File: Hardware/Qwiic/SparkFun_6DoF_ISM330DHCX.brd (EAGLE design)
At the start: 25.4 x 25.4 mm, 64 parts, among them J1 QWIIC_RIGHT_ANGLE, J2 QWIIC_RIGHT_ANGLE, U1 ISM330DHCX

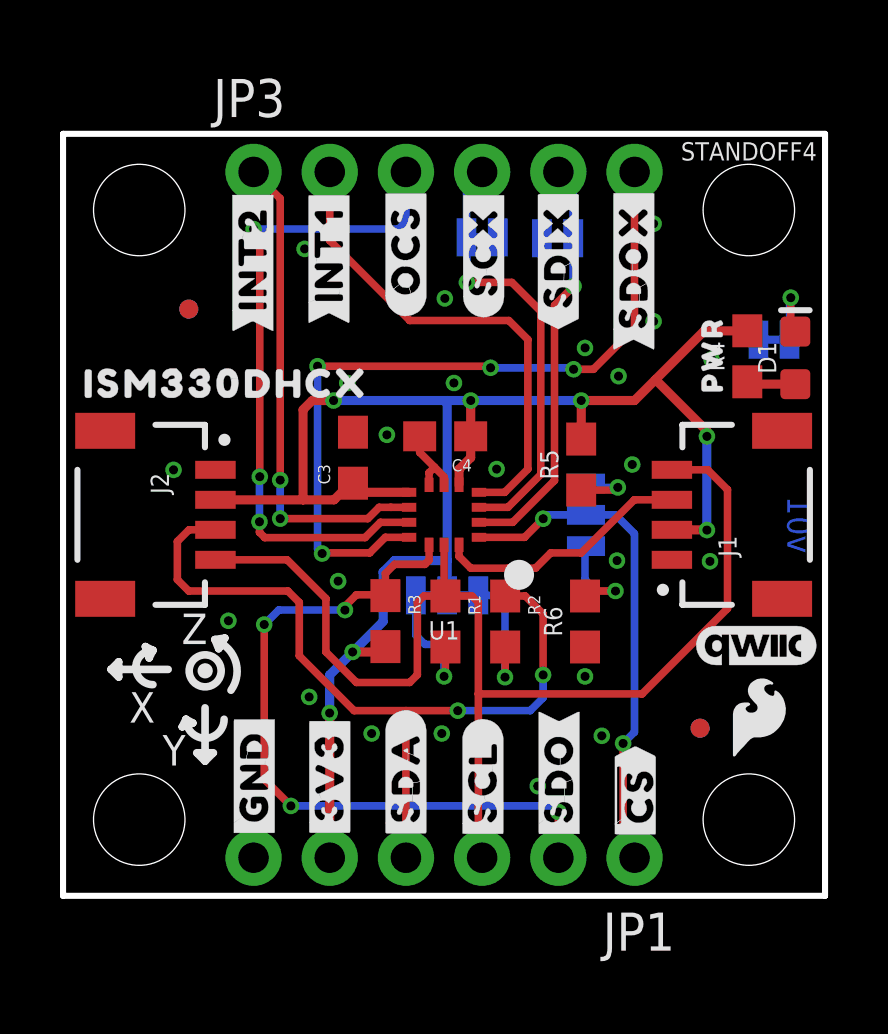
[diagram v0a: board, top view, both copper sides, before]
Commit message: Updates labels on 1x1 to new SPI nomenclature,
* moves pin1 indicator on IC closer to IC
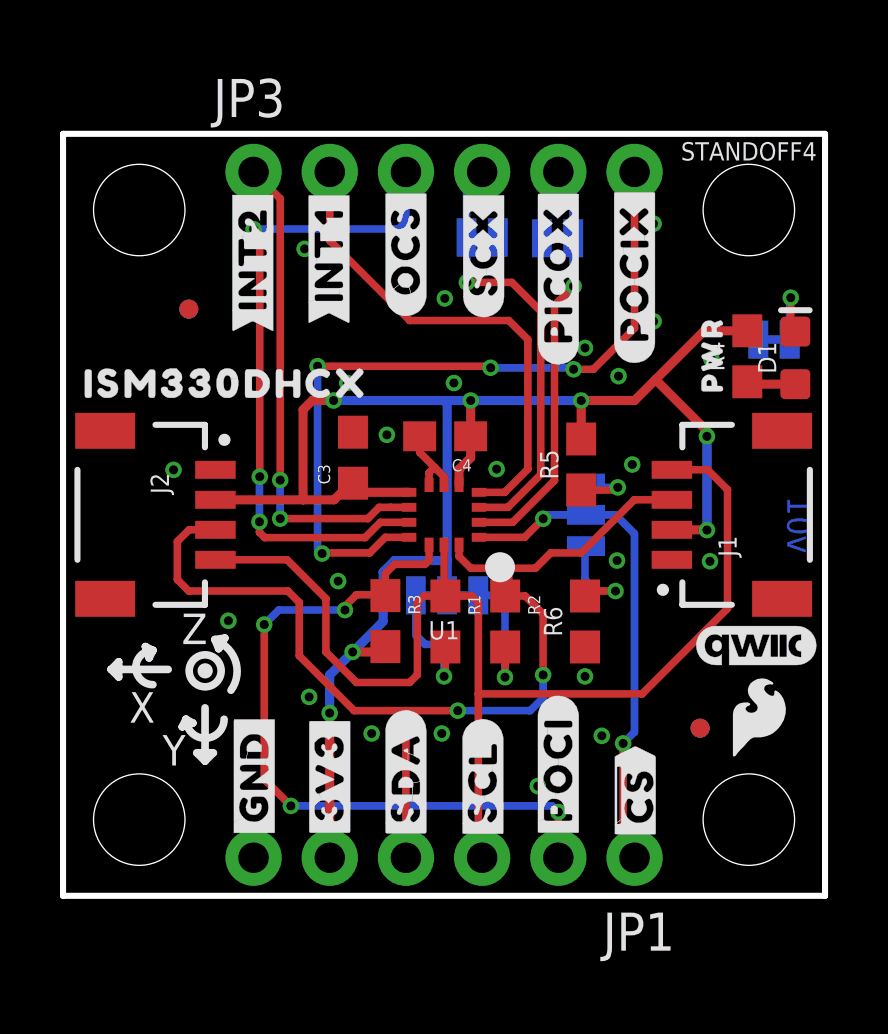
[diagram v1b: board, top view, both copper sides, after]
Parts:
- U$11: device top:#SDIX#11 -> ISMTop:#PICOX#10
- U$18: device bot:#SDO#7 -> ISMTop:#POCI#12
- U$24: device top:#SDOX#12 -> ISMTop:#POCIX#8
- U$26: device bot:#SDI#4 -> ISMTop:#PICO#13
- U$32: device bot:#SDOX#12 -> ISMTop:#PICOX#9
- U$33: device bot:#SDIX#11 -> ISMTop:#POCIX#7
- U$6: device top:#SDO#6 -> ISMTop:#POCI#11
- moved U$32 3.77 mm to (16.5, 18.2)
- moved U$33 3.21 mm to (19.1, 20.8)
- moved U$11 0.58 mm to (16.5, 20.7)
- moved U$26 0.56 mm to (11.4, 4.17)
- moved U$18 0.28 mm to (16.5, 4.22), flipped to the top, turned to 90 degrees
- moved U$6 0.28 mm to (16.5, 4.22), flipped to the bottom, turned to 270 degrees
- moved U$24 0.20 mm to (19.1, 20.8)
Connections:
- net SDA renamed SDA/PICO
- net SDI_AUX renamed PICO_AUX
- net SDO/SA0 renamed POCI/SA0
- net SDO_AUX renamed POCI_AUX
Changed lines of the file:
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@@
 <drawing>
 <settings>
-<setting alwaysvectorfont="yes"/>
+<setting alwaysvectorfont="no"/>
 <setting keepoldvectorfont="yes"/>
 <setting verticaltext="up"/>
@@
 <element name="U$7" library="top" package="#INT1#9" value="" x="8.8646" y="21.3868" smashed="yes" rot="R90"/>
 <element name="U$8" library="top" package="#INT2#9" value="" x="6.3246" y="21.2598" smashed="yes" rot="R90"/>
-<element name="U$6" library="top" package="#SDO#6" value="" x="16.5354" y="3.937" smashed="yes" rot="R90"/>
-<element name="U$18" library="bot" package="#SDO#7" value="" x="16.5354" y="3.937" smashed="yes" rot="MR270"/>
 <element name="U$19" library="bot" package="#INT1#9" value="" x="8.8646" y="21.3868" smashed="yes" rot="MR270"/>
 <element name="U$21" library="bot" package="#INT2#9" value="" x="6.3246" y="21.2598" smashed="yes" rot="MR270"/>
-<element name="U$26" library="bot" package="#SDI#4" value="" x="11.43" y="3.6068" smashed="yes" rot="MR270"/>
 <element name="STANDOFF4" library="SparkFun-Hardware" package="STAND-OFF-TIGHT" value="STAND-OFFTIGHT" x="22.86" y="22.86" smashed="yes">
 <attribute name="NAME" x="22.86" y="24.511" size="0.6096" layer="25" font="vector" ratio="20" align="bottom-center"/>
@@
 </element>
 <element name="U$29" library="SparkFun-Aesthetics" package="SFE_LOGO_FLAME_.1" value="" x="23.1902" y="5.969" smashed="yes"/>
-<element name="U$11" library="top" package="#SDIX#11" value="" x="16.51" y="21.3106" smashed="yes" rot="R90"/>
-<element name="U$24" library="top" package="#SDOX#12" value="" x="19.0246" y="20.9804" smashed="yes" rot="R90"/>
-<element name="U$32" library="bot" package="#SDOX#12" value="" x="19.0246" y="21.0058" smashed="yes" rot="MR270"/>
-<element name="U$33" library="bot" package="#SDIX#11" value="" x="16.51" y="18.8214" smashed="yes" rot="MR270"/>
 <element name="U1" library="ISM330DHCX" package="LGA-14L" value="ISM330DHCX" x="12.7" y="12.7" smashed="yes" rot="R180">
 <attribute name="NAME" x="12.7" y="8.851" size="0.6096" layer="25" font="vector" ratio="20" rot="R180" align="center"/>
@@
 <element name="U$12" library="ISMTop" package="ISM330DHCX331" value="" x="5.4356" y="17.0688" smashed="yes"/>
 <element name="U$30" library="ISMTop" package="ISM330DHCX20" value="" x="7.5184" y="12.8524" smashed="yes" rot="MR270"/>
+<element name="U$11" library="ISMTop" package="#PICOX#10" value="" x="16.51" y="20.7264" smashed="yes" rot="R90"/>
+<element name="U$24" library="ISMTop" package="#POCIX#8" value="" x="19.05" y="20.7772" smashed="yes" rot="R90"/>
+<element name="U$32" library="ISMTop" package="#PICOX#9" value="" x="16.4592" y="18.2372" smashed="yes" rot="MR270"/>
+<element name="U$33" library="ISMTop" package="#POCIX#7" value="" x="19.05" y="20.7772" smashed="yes" rot="MR270"/>
+<element name="U$26" library="ISMTop" package="#PICO#13" value="" x="11.43" y="4.1656" smashed="yes" rot="MR270"/>
+<element name="U$6" library="ISMTop" package="#POCI#11" value="" x="16.51" y="4.2164" smashed="yes" rot="MR270"/>
+<element name="U$18" library="ISMTop" package="#POCI#12" value="" x="16.51" y="4.2164" smashed="yes" rot="R90"/>
 </elements>
 <signals>
@@
 <wire x1="13.843" y1="6.731" x2="13.843" y2="1.397" width="0.254" layer="1"/>
 </signal>
-<signal name="SDA">
+<signal name="SDA/PICO">
 <contactref element="JP1" pad="4"/>
 <contactref element="J1" pad="3"/>
@@
 <wire x1="7.5946" y1="2.9972" x2="6.7056" y2="3.8862" width="0.254" layer="1"/>
 </signal>
-<signal name="SDO/SA0">
+<signal name="POCI/SA0">
 <contactref element="ADDR" pad="2"/>
 <contactref element="U1" pad="P1"/>
@@
 <wire x1="19.0476" y1="12.0674" x2="19.0476" y2="5.4586" width="0.254" layer="16"/>
 </signal>
-<signal name="SDI_AUX">
+<signal name="PICO_AUX">
 <contactref element="JP3" pad="5"/>
 <contactref element="SDX" pad="2"/>
@@
 <wire x1="17.55775" y1="13.6144" x2="17.43075" y2="13.7414" width="0.254" layer="16"/>
 </signal>
-<signal name="SDO_AUX">
+<signal name="POCI_AUX">
 <contactref element="JP3" pad="6"/>
 <contactref element="U1" pad="P11"/>

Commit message: Moves some vias, fixes "x", "y", and "z" on axes, fixes some schematic typos
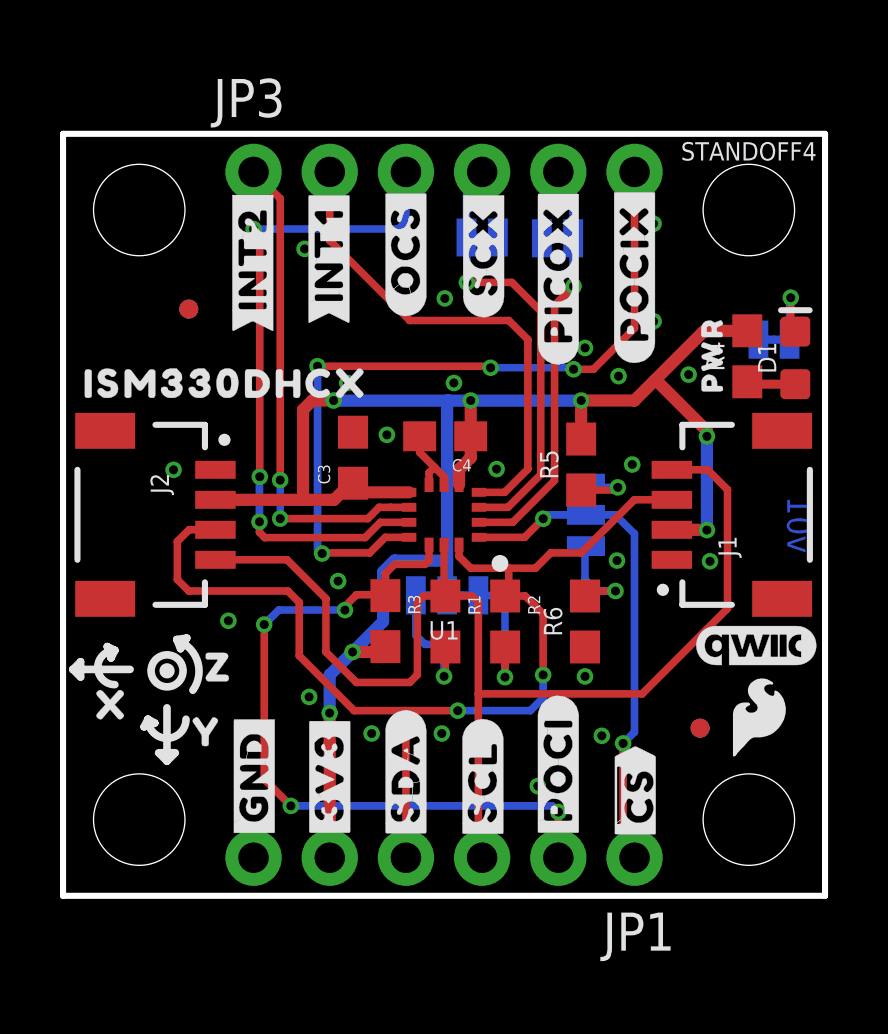
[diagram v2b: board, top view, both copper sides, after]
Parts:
- added U$34, U$37: (no value), ISMTopMini:X2114
- added U$35, U$38: (no value), ISMTopMini:Y2115
- added U$36, U$39: (no value), ISMTopMini:Z2116
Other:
- board text removed: "X"
- board text removed: "Y"
- board text removed: "Z"
